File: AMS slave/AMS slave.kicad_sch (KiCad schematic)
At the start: 48 parts, among them J2 Conn_02x03_Odd_Even, J3 Conn_01x05, J4 Conn_01x05, Q2 AO3402, Q3 NCE60P04Y, SW2 SW_Push, U2 ATmega328P-A, U3 MCP2515-xST, U4 ISO1050DUB, U5 B0505S-2WR3, Y1 20MHz, Y2 8MHz

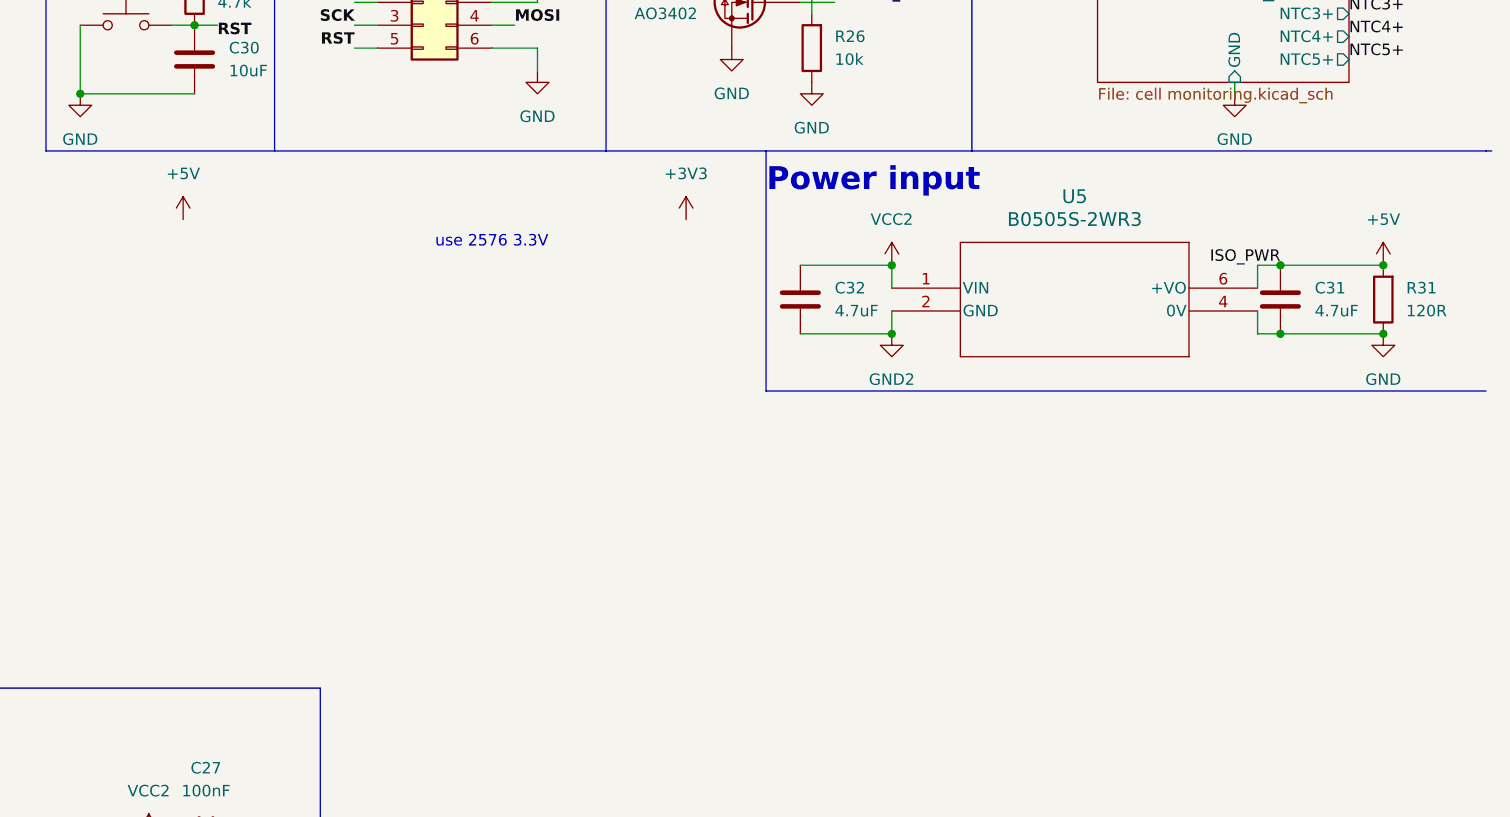
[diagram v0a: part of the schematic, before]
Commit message: fixed VTAP collisions, AMS slave redesign WIP
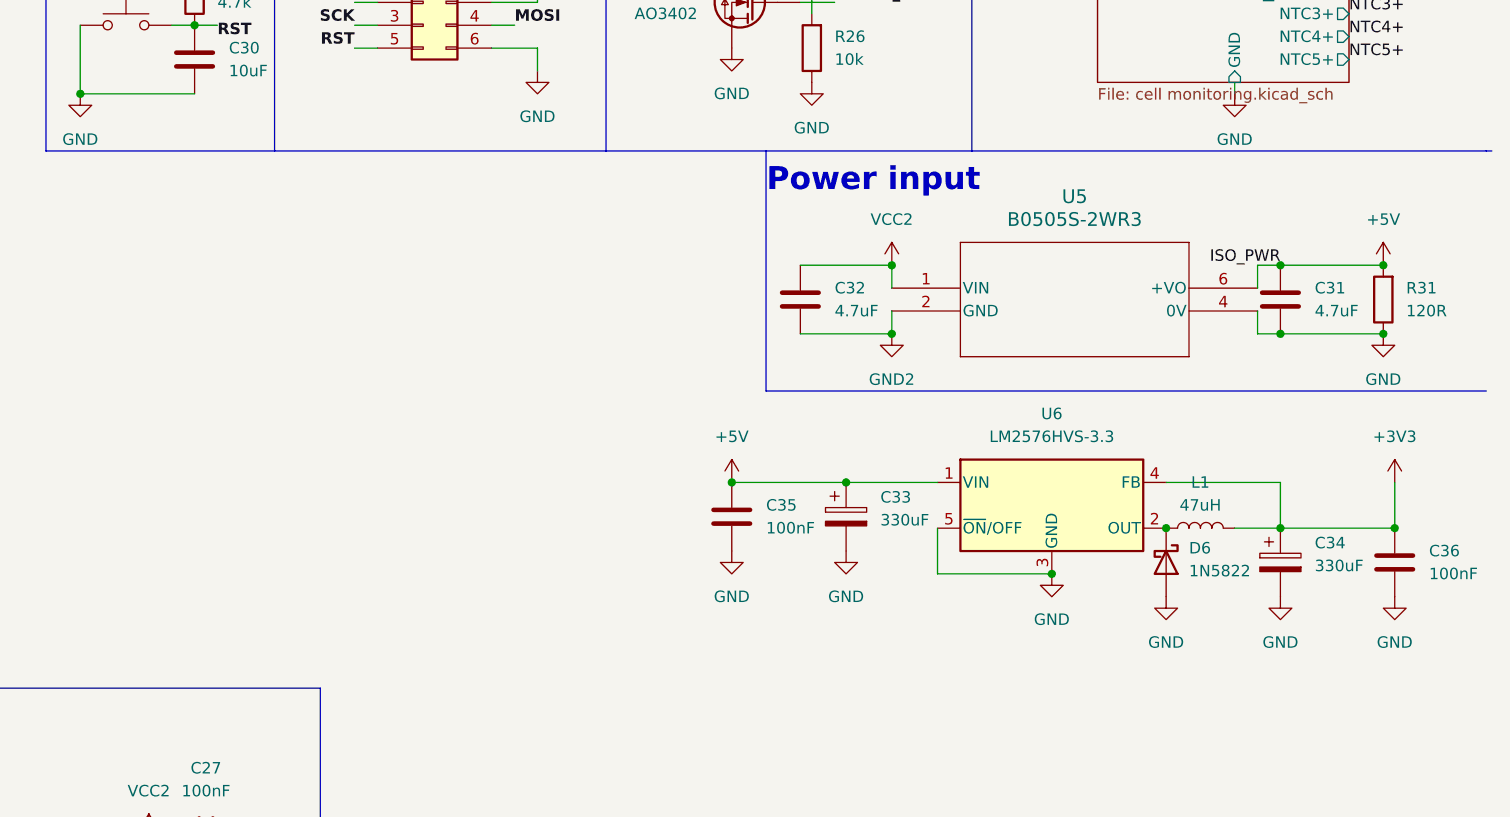
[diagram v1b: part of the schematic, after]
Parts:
- added C33, C34: 330uF, symbol Device:C_Polarized
- added C35, C36: 100nF, RMC_Capacitor:C_0805_2012Metric_Pad1.18x1.45mm_HandSolder_L, symbol Device:C
- added D6: 1N5822, Diode_THT:D_DO-201AD_P15.24mm_Horizontal, symbol Diode:1N5822
- added L1: 47uH, symbol Device:L
- added U6: LM2576HVS-3.3, Package_TO_SOT_SMD:TO-263-5_TabPin3, symbol Regulator_Switching:LM2576HVS-3.3
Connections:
- net +3V3: now also C34.1, C36.2, L1.2, U6.4 (FB)
- net +5V: now also C33.1, C35.2, U6.1 (VIN)
- net GND: now also C33.2, C34.2, C35.1, C36.1, D6.2 (A), U6.3 (GND), U6.5 (~{ON}/OFF)
- new net: D6.1 (K), L1.1, U6.2 (OUT)
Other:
- note removed: "use 2576 3.3V"

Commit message: VTAP trace corners fixed
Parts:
- C33, C34: footprint (none) -> RMC_Capacitor:CP_Radial_D6.3mm_P2.50mm_handsolder
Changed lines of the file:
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@@
 			)
 		)
-		(property "Footprint" ""
+		(property "Footprint" "RMC_Capacitor:CP_Radial_D6.3mm_P2.50mm_handsolder"
 			(at 214.3252 114.3 0)
 			(effects
@@
 			)
 		)
-		(property "Footprint" ""
+		(property "Footprint" "RMC_Capacitor:CP_Radial_D6.3mm_P2.50mm_handsolder"
 			(at 262.5852 119.38 0)
 			(effects

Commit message: AMS slave WIP
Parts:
- L1: footprint (none) -> RMC_Inductor:L_10.4x10.4_H4.8_handsolder
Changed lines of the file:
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@@
 			)
 		)
-		(property "Footprint" ""
+		(property "Footprint" "RMC_Inductor:L_10.4x10.4_H4.8_handsolder"
 			(at 252.73 111.76 0)
 			(effects

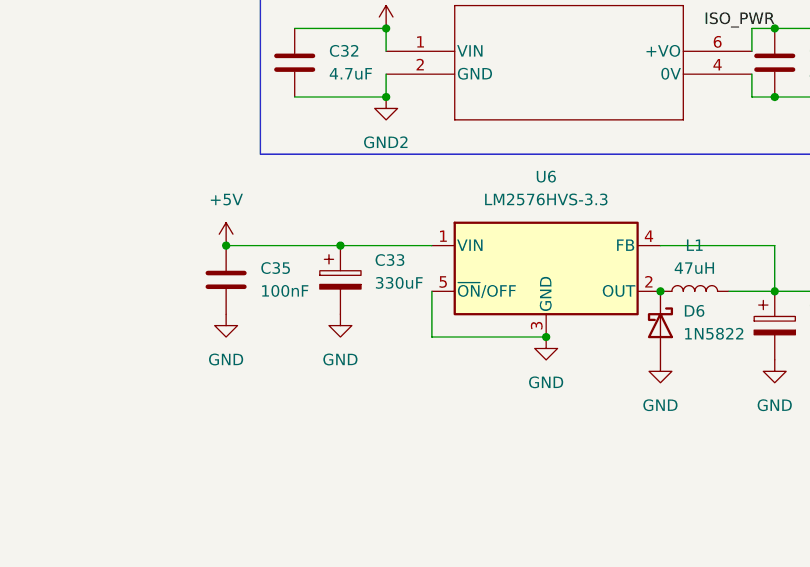
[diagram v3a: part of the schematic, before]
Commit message: AMS slave schem updated
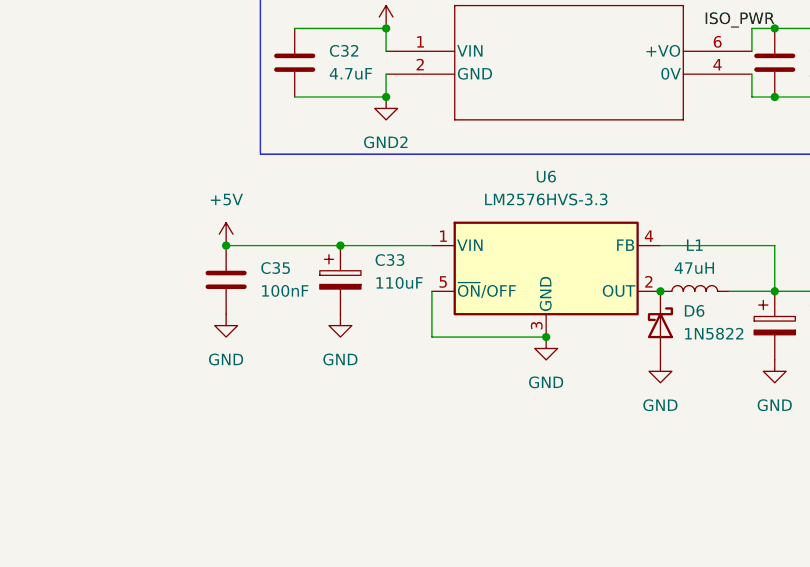
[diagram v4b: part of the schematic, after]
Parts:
- C33: value 330uF -> 110uF
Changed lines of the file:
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@@
 			)
 		)
-		(property "Value" "330uF"
+		(property "Value" "110uF"
 			(at 217.17 110.8709 0)
 			(effects

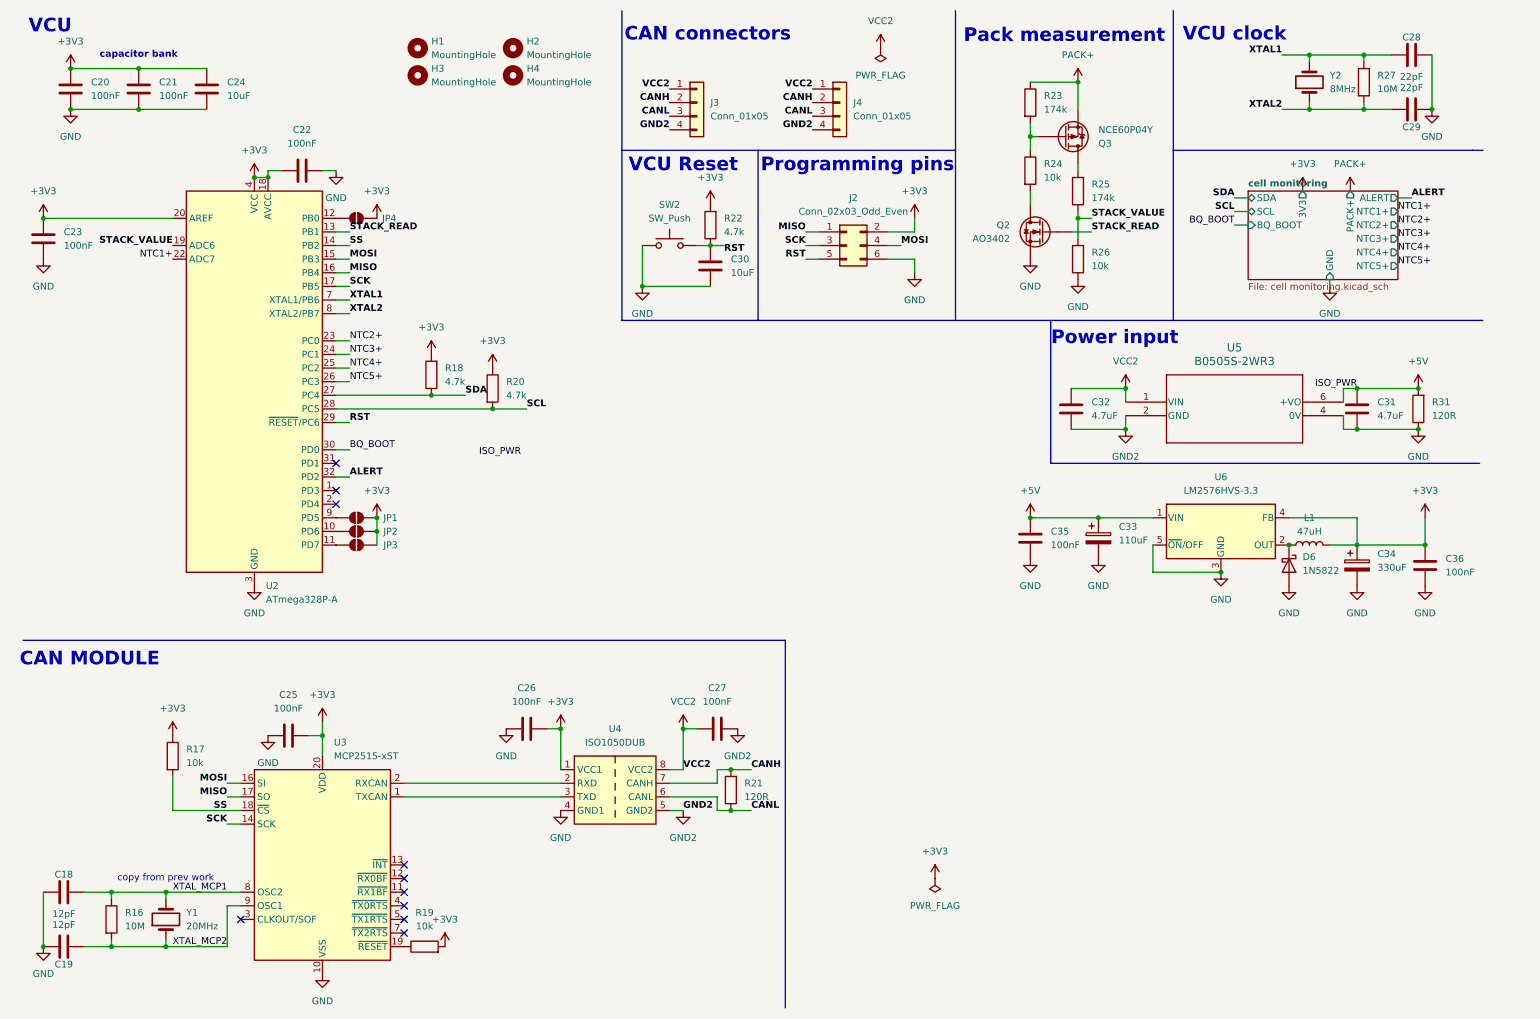
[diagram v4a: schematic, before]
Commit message: AMS slave schem 0.5.0 pcb 0.6.0, VTAP silkscreen
AMS slave changed to account for architectural changes
Schematic changes:
- power is now provided mainly through the 5V CAN input with voltage isolation
- BQ76940 thermistors moved to mcu
PCB changes:
- board to board connector requires all components to be on top surface
VTAP changes:
Added silkscreen to indicate cell and pack polarity
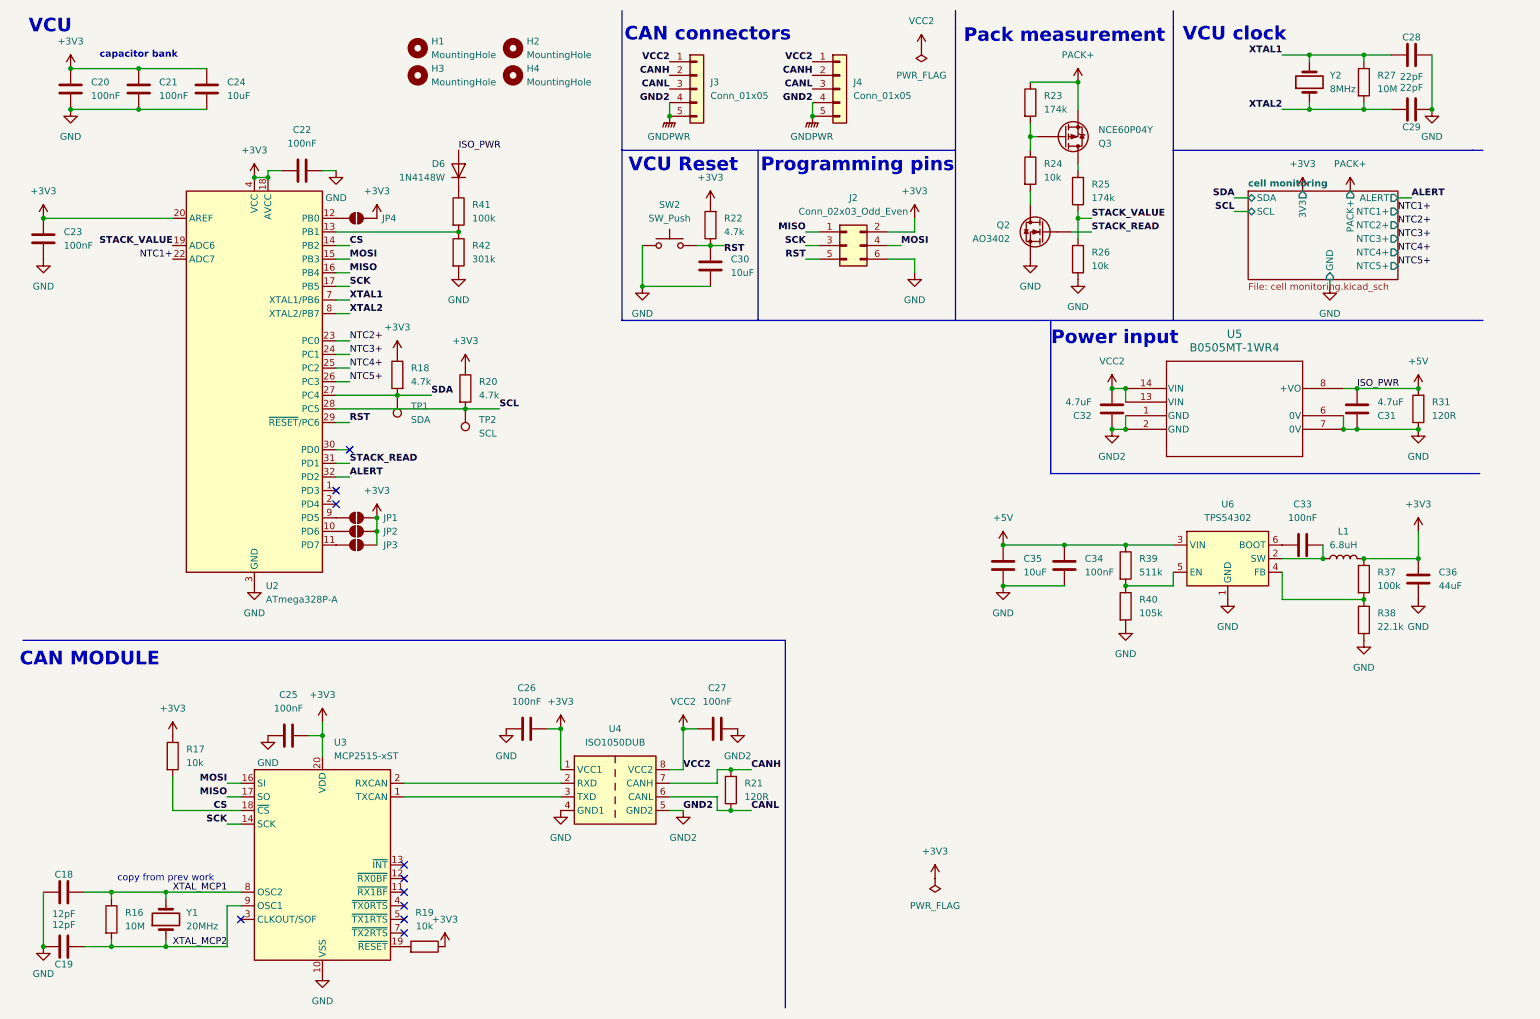
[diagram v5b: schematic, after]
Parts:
- removed C33: 110uF, RMC_Capacitor:CP_Radial_D6.3mm_P2.50mm_handsolder, symbol Device:C_Polarized
- removed C34: 330uF, RMC_Capacitor:CP_Radial_D6.3mm_P2.50mm_handsolder, symbol Device:C_Polarized
- removed D6: 1N5822, Diode_THT:D_DO-201AD_P15.24mm_Horizontal, symbol Diode:1N5822
- removed U5: B0505S-2WR3, B0505S-2W3R:B_S-2WR2_MNS, symbol B0505S-2W3R:B0505S-2WR3
- removed U6: LM2576HVS-3.3, Package_TO_SOT_SMD:TO-263-5_TabPin3, symbol Regulator_Switching:LM2576HVS-3.3
- added C33, C34: 100nF, RMC_Capacitor:C_0805_2012Metric_Pad1.18x1.45mm_HandSolder_L, symbol Device:C
- added D6: 1N4148W, Diode_SMD:D_0805_2012Metric_Pad1.15x1.40mm_HandSolder, symbol Device:D
- added R37, R41: 100k, RMC_Resistor:R_0805_2012Metric_Pad1.20x1.40mm_HandSolder_L, symbol Device:R
- added R38: 22.1k, RMC_Resistor:R_0805_2012Metric_Pad1.20x1.40mm_HandSolder_L, symbol Device:R
- added R39: 511k, RMC_Resistor:R_0805_2012Metric_Pad1.20x1.40mm_HandSolder_L, symbol Device:R
- added R40: 105k, RMC_Resistor:R_0805_2012Metric_Pad1.20x1.40mm_HandSolder_L, symbol Device:R
- added R42: 301k, RMC_Resistor:R_0805_2012Metric_Pad1.20x1.40mm_HandSolder_L, symbol Device:R
- added TP1: SDA, TestPoint:TestPoint_Pad_2.5x2.5mm, symbol Connector:TestPoint
- added TP2: SCL, TestPoint:TestPoint_Pad_2.5x2.5mm, symbol Connector:TestPoint
- added U5: B0505MT-1WR4, B05xxMT-1WR4_MNS:B05xxMT-1WR4_MNS, symbol B05xxMT-1WR4_MNS:B0505MT-1WR4
- added U6: TPS54302, Package_TO_SOT_SMD:SOT-23-6, symbol Regulator_Switching:TPS54302
- C35: value 100nF -> 10uF
- C36: value 100nF -> 44uF
- J2: footprint Connector_PinHeader_2.54mm:PinHeader_2x03_P2.54mm_Vertical -> Connector_PinHeader_2.54mm:PinHeader_2x03_P2.54mm_Vertical_SMD
- J3, J4: footprint Connector_Molex:Molex_Micro-Fit_3.0_43650-0415_1x04_P3.00mm_Vertical -> Connector_Molex:Molex_Micro-Fit_3.0_43650-0521_1x05_P3.00mm_Vertical; symbol Connector_Generic:Conn_01x04 -> Connector_Generic:Conn_01x05
- L1: value 47uH -> 6.8uH; footprint RMC_Inductor:L_10.4x10.4_H4.8_handsolder -> Inductor_SMD:L_6.3x6.3_H3
- Y1, Y2: footprint Crystal:Crystal_HC49-U_Vertical -> RMC_Crystal:Crystal_HC49-U_Vertical_W_SMD_Handolder
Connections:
- net +3V3: now also C36.1, R18.1, R19.1, R37.1; no longer C36.2, R18.2, R19.2
- net +5V: now also C31.1, C35.1, C34.1, D6.2 (A), R39.1, U5.8 (+VO), U6.3 (VIN); no longer C31.2, C35.2
- net GND: now also C31.2, C35.2, C36.2, C34.2, R38.2, R40.2, R42.2, U5.6 (0V), U5.7 (0V), U6.1 (GND); no longer C31.1, C35.1, C36.1
- net GND2: now also C32.1, J3.5 (Pin_5), J4.5 (Pin_5), U5.1 (GND), U5.2 (GND); no longer C32.2
- net SCL: now also TP2.1
- net SDA: now also R18.2, TP1.1; no longer R18.1
- net STACK_READ: now also U2.31 (PD1); no longer U2.13 (PB1)
- net VCC2: now also C32.2, U5.13 (VIN), U5.14 (VIN); no longer C32.1
- net at U3.19 (~{RESET}): now also R19.2; no longer R19.1
- net at L1.1: now also C33.1, U6.2 (SW)
- net BQ_BOOT: no longer names the net of U2.30 (PD0)
- net SS renamed CS
- new net: D6.1 (K), R41.1
- new net: R41.2, R42.1, U2.13 (PB1)
- new net: R37.2, R38.1, U6.4 (FB)
- new net: R39.2, R40.1, U6.5 (EN)
- new net: C33.2, U6.6 (BOOT)
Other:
- sheet cell monitoring ports: added none; removed BQ_BOOT
- moved on the sheet: C31, C32, R18, R19, R20

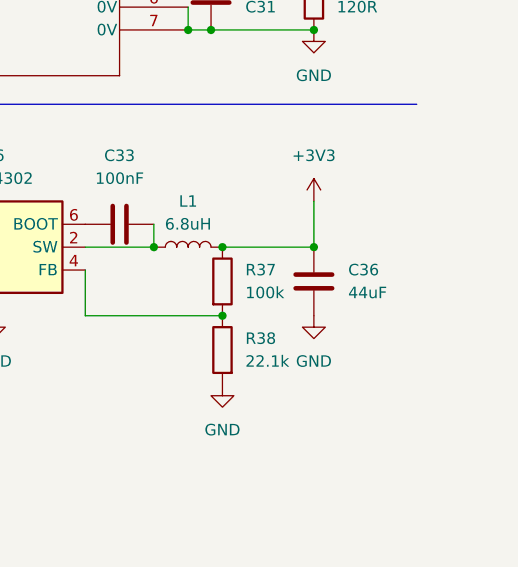
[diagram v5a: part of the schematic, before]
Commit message: AMS slave minor corrections
Added a second pad for AMS slave for future soldering, updated BOM
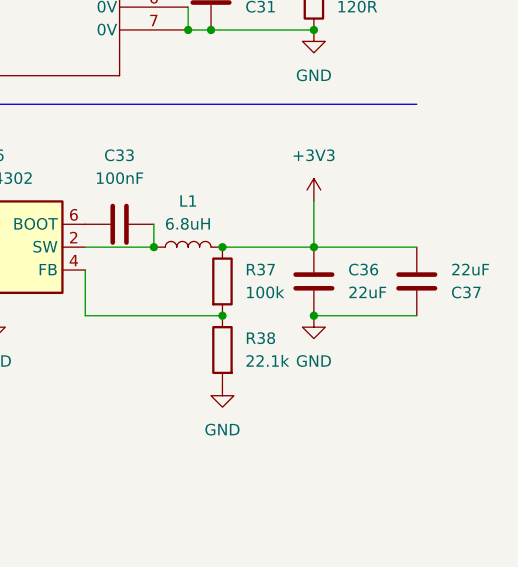
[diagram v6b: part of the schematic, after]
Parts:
- added C37: 22uF, RMC_Capacitor:C_0805_2012Metric_Pad1.18x1.45mm_HandSolder_L, symbol Device:C
- C36: value 44uF -> 22uF
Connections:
- net +3V3: now also C37.2
- net GND: now also C37.1

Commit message: Added two pin connections
lazy
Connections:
- net +3V3: now also C37.1; no longer C37.2
- net GND: now also C37.2; no longer C37.1
- net ~{RX0BF}: now reaches U3.12 (~{RX0BF})
- net ~{RX0BF}: now also U2.1 (PD3)
- net ~{INT}: now reaches U3.13 (~{INT})
- net ~{INT}: now also U2.2 (PD4)
- no-connect marks 10 -> 6
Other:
- moved on the sheet: JP1, JP2, JP3, Q2, Q3, R23, R24, R25, R26
